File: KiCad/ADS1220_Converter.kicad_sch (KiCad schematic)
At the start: 15 parts, among them U2 ADS1220xPW

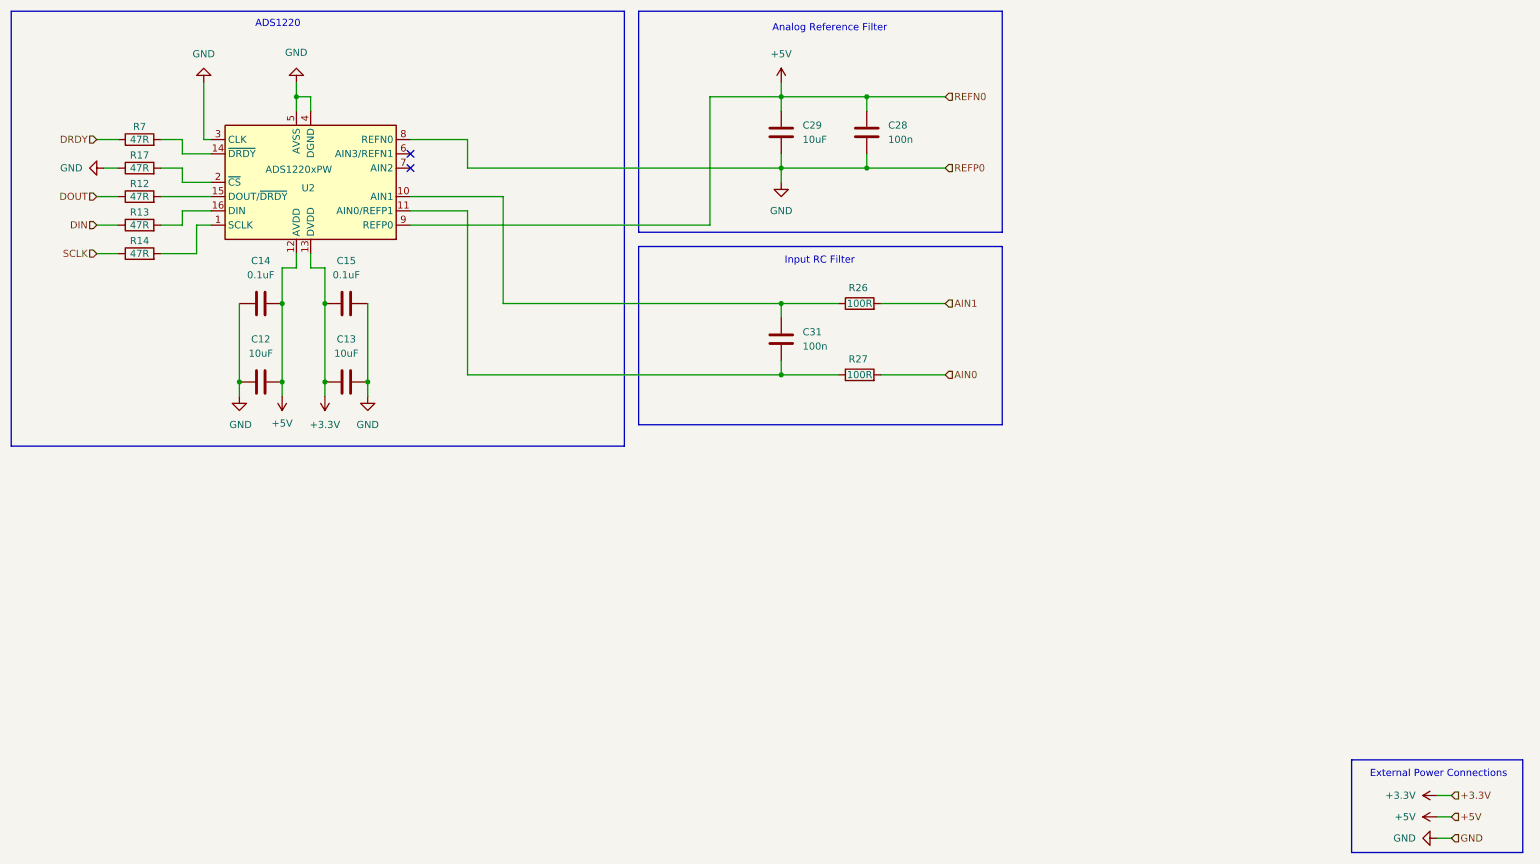
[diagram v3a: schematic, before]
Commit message: Convert Power to LDOs
Convert power section to use only LDOs. This means we will only get 4.75V or 4.5V on the analog line but this comes with greatly increased simplicity of layout.
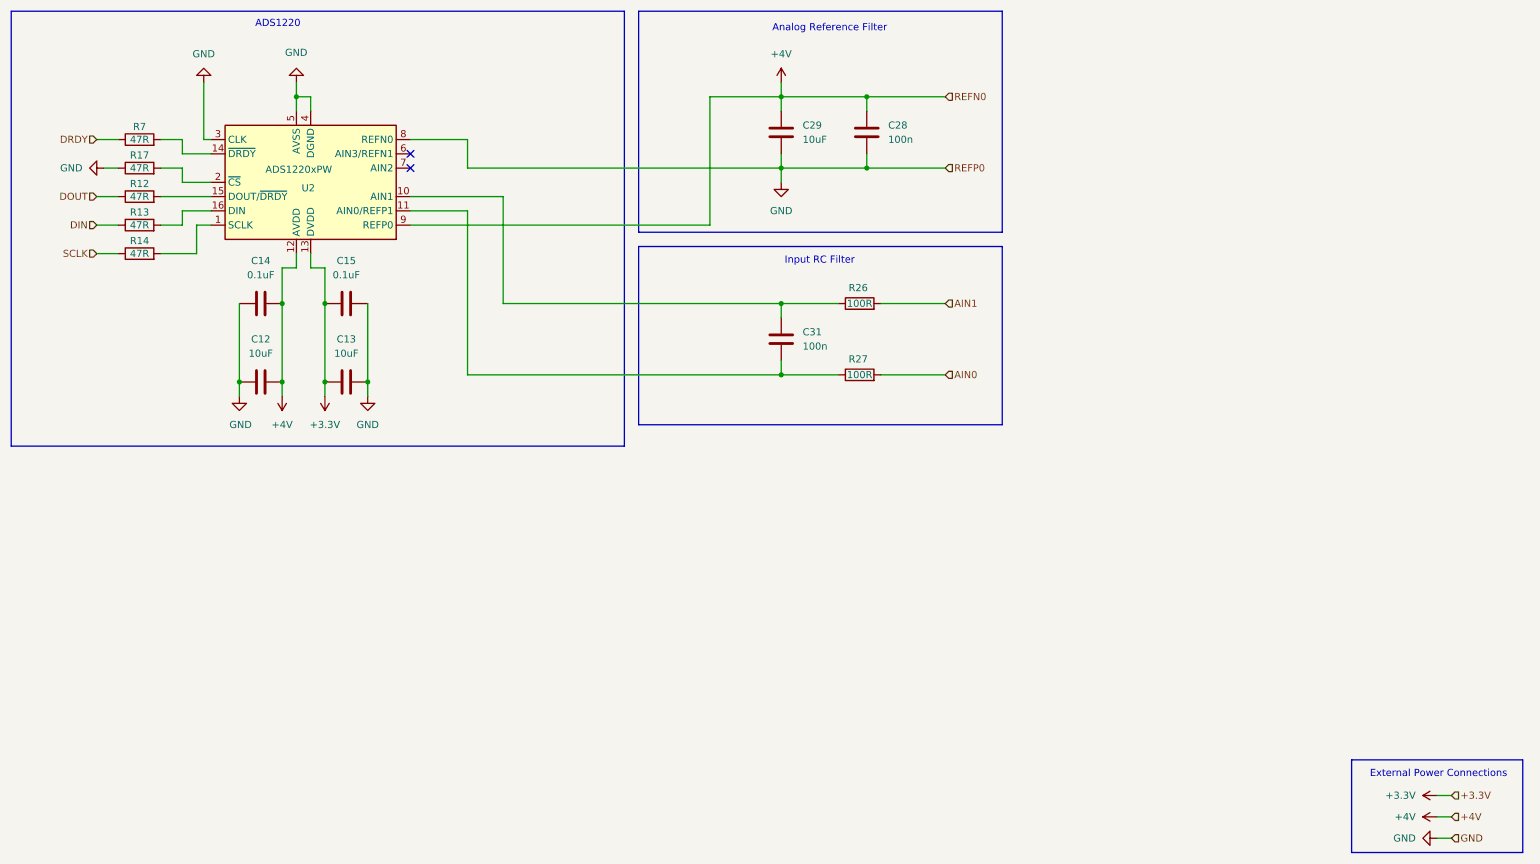
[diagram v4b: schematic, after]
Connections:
- net +5V renamed +4V

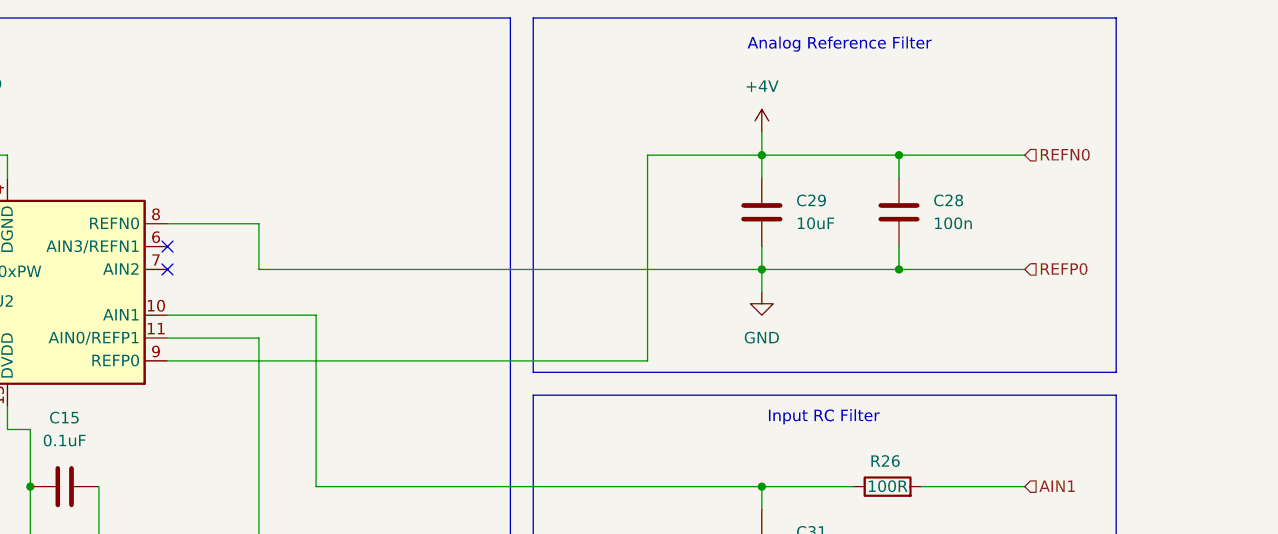
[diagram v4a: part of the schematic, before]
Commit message: Add Single Wire Debug
* Add Single Wire Debug (SWD) Tag Connect Connector
* Re-layout of 5V power so the 5V pins connect to a pad directly behind the USB connector
* Add 0R resistors to air gap the 3.3V and 5V power rails for incremental board bringup
* Rotate ADS1220 for cleaner layout
* Remove connections to reference voltage pins, since AVDD/AVSS is a valid reference

fixup

fixup

fixup
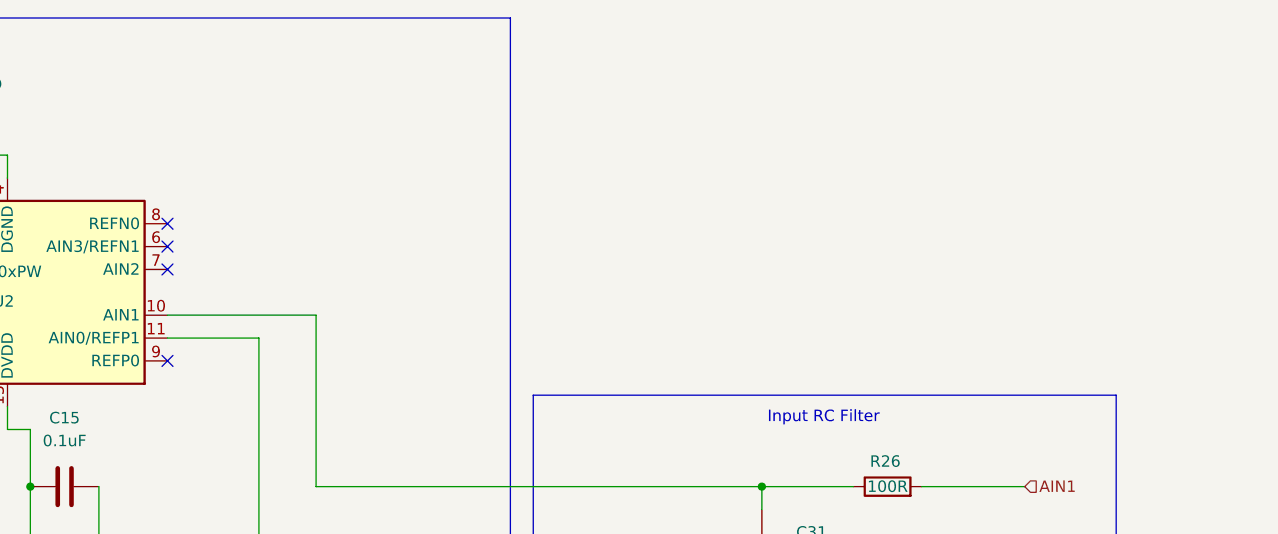
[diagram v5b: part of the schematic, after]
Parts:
- removed C28: 100n, Capacitor_SMD:C_0805_2012Metric_Pad1.18x1.45mm_HandSolder, symbol Device:C
- removed C29: 10uF, Capacitor_SMD:C_0805_2012Metric_Pad1.18x1.45mm_HandSolder, symbol Device:C
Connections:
- net +4V: no longer U2.9 (REFP0)
- net GND: no longer U2.8 (REFN0)
- no-connect marks 2 -> 4
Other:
- note removed: "Analog Reference Filter"

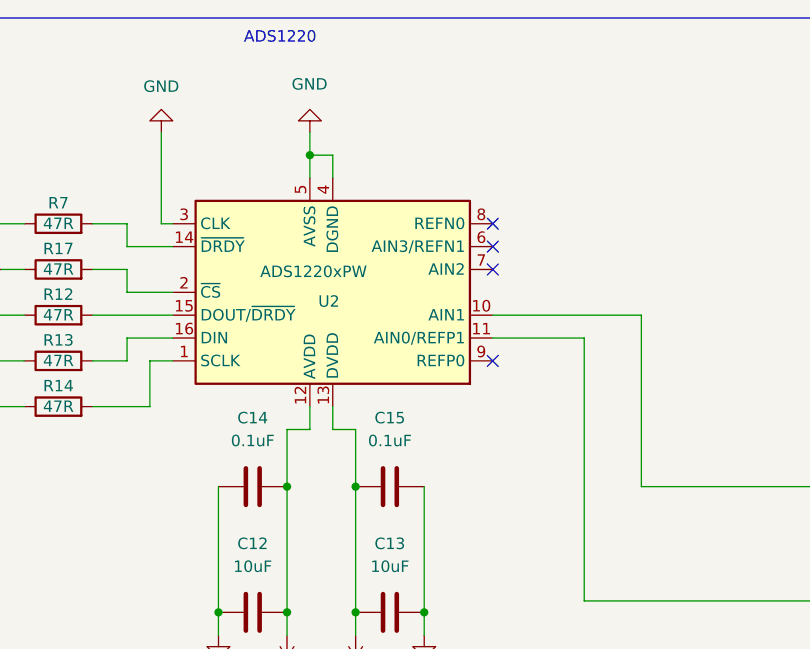
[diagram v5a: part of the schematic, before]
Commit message: Crystal Changes
* Update crystal selection, schematic and footprint
* Add resistor to limit drive current to crystal
* Block ground plane fill under crystal circuit
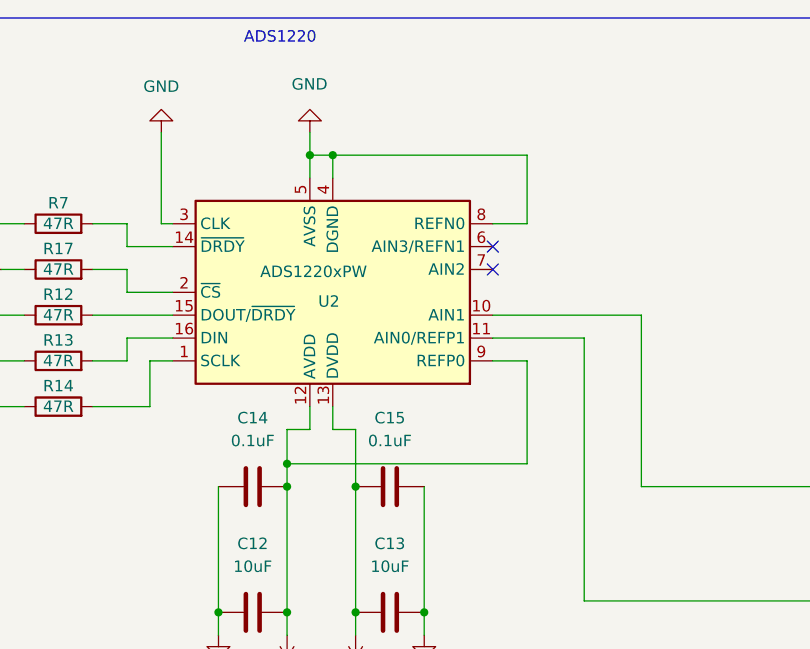
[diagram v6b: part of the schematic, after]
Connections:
- net +4V: now also U2.9 (REFP0)
- net GND: now also U2.8 (REFN0)
- no-connect marks 4 -> 2
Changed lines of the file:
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@@
+	)
+	(junction
+		(at 67.31 29.21)
+		(diameter 0)
+		(color 0 0 0 0)
 	)
 	(junction
@@
 	(junction
 		(at 69.85 66.04)
+		(diameter 0)
+		(color 0 0 0 0)
+	)
+	(junction
+		(at 62.23 63.5)
 		(diameter 0)
 		(color 0 0 0 0)
@@
 		(at 85.09 41.91)
 	)
-	(no_connect
-		(at 85.09 52.07)
-	)
-	(no_connect
-		(at 85.09 36.83)
-	)
 	(wire
 		(pts
@@
 	(wire
 		(pts
+			(xy 62.23 63.5) (xy 62.23 66.04)
+		)
+		(stroke
+			(width 0)
+			(type default)
+		)
+	)
+	(wire
+		(pts
+			(xy 88.9 52.07) (xy 85.09 52.07)
+		)
+		(stroke
+			(width 0)
+			(type default)
+		)
+	)
+	(wire
+		(pts
+			(xy 88.9 29.21) (xy 88.9 36.83)
+		)
+		(stroke
+			(width 0)
+			(type default)
+		)
+	)
+	(wire
+		(pts
 			(xy 40.64 52.07) (xy 44.45 52.07)
 		)
@@
 	(wire
 		(pts
+			(xy 67.31 29.21) (xy 88.9 29.21)
+		)
+		(stroke
+			(width 0)
+			(type default)
+		)
+	)
+	(wire
+		(pts
 			(xy 69.85 59.69) (xy 69.85 66.04)
 		)
@@
 	(wire
 		(pts
+			(xy 88.9 36.83) (xy 85.09 36.83)
+		)
+		(stroke
+			(width 0)
+			(type default)
+		)
+	)
+	(wire
+		(pts
+			(xy 62.23 63.5) (xy 88.9 63.5)
+		)
+		(stroke
+			(width 0)
+			(type default)
+		)
+	)
+	(wire
+		(pts
 			(xy 29.21 57.15) (xy 33.02 57.15)
 		)
@@
 	(wire
 		(pts
-			(xy 62.23 59.69) (xy 62.23 66.04)
+			(xy 62.23 59.69) (xy 62.23 63.5)
 		)
 		(stroke
@@
 		)
 		(stroke
+			(width 0)
+			(type default)
+		)
+	)
+	(wire
+		(pts
+			(xy 88.9 63.5) (xy 88.9 52.07)
+		)
+		(stroke

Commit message: Work In Progress
moving towards v 2
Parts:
- added C5, C6: 10uF, Capacitor_SMD:C_0805_2012Metric_Pad1.18x1.45mm_HandSolder, symbol Device:C
- added C7, C8: 0.1uF, Capacitor_SMD:C_0805_2012Metric_Pad1.18x1.45mm_HandSolder, symbol Device:C
- added R18, R21: 100R, Resistor_SMD:R_0805_2012Metric_Pad1.20x1.40mm_HandSolder, symbol Device:R
- C31: value 100n -> 0.1uF
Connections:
- net +4V: now also R18.2; no longer U2.9 (REFP0)
- net GND: now also C7.1, C8.2, R21.2; no longer U2.8 (REFN0)
- net at C31.1, R26.1, U2.10 (AIN1): now also C7.2
- net at C31.2, R27.1, U2.11 (AIN0/REFP1): now also C8.1
- new net: C5.2, C6.2, R21.1, U2.9 (REFP0)
- new net: C5.1, C6.1, R18.1, U2.8 (REFN0)
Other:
- note added: "Reference RC Filter"
- moved on the sheet: C31, R26, R27
